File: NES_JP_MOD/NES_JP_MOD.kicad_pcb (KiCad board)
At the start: 2 copper layers, 9 parts, among them J1 Conn_01x06, U1 XC2C64A, U2 AMS1117-1.8, U3 AMS1117-3.3, X1 ASV-xxxMHz

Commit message: Created PCB
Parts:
- added C5: 0.1u, Capacitor_SMD:C_0805_2012Metric, F.Cu at (129.3, 89.2)
- added C6: 0.1u, Capacitor_SMD:C_0805_2012Metric, F.Cu at (129.3, 93.7)
- added C7: 0.1u, Capacitor_SMD:C_0805_2012Metric, F.Cu at (138.4, 98.0)
- added C8: 0.1u, Capacitor_SMD:C_0805_2012Metric, F.Cu at (147.3, 92.2)
- added C9: 0.1u, Capacitor_SMD:C_0805_2012Metric, F.Cu at (133.3, 87.6)
- added Q1: MMBT3904, Package_TO_SOT_SMD:SOT-23, F.Cu at (152.4, 78.7)
- added R1: 5K6, Resistor_SMD:R_0805_2012Metric, F.Cu at (151.9, 83.8)
- added R10: 10K, Resistor_SMD:R_0805_2012Metric, F.Cu at (143.0, 102.1)
- added R11: 10K, Resistor_SMD:R_0805_2012Metric, F.Cu at (139.0, 102.1)
- added R12: 5K6, Resistor_SMD:R_0805_2012Metric, F.Cu at (152.7, 91.2)
- added R13: 10K, Resistor_SMD:R_0805_2012Metric, F.Cu at (150.4, 91.2)
- added R14: 10K, Resistor_SMD:R_0805_2012Metric, F.Cu at (134.9, 102.1)
- added R15: 10K, Resistor_SMD:R_0805_2012Metric, F.Cu at (130.8, 102.1)
- added R16: 10K, Resistor_SMD:R_0805_2012Metric, F.Cu at (126.7, 102.1)
- added R17: 10K, Resistor_SMD:R_0805_2012Metric, F.Cu at (122.7, 102.1)
- added R18: 10K, Resistor_SMD:R_0805_2012Metric, F.Cu at (118.6, 102.1)
- added R2: 10K, Resistor_SMD:R_0805_2012Metric, F.Cu at (149.2, 78.5)
- added R3: 10K, Resistor_SMD:R_0805_2012Metric, F.Cu at (154.9, 97.8)
- added R4: 10K, Resistor_SMD:R_0805_2012Metric, F.Cu at (157.5, 97.8)
- added R5: 10K, Resistor_SMD:R_0805_2012Metric, F.Cu at (156.7, 102.1)
- added R6: 10K, Resistor_SMD:R_0805_2012Metric, F.Cu at (152.7, 102.1)
- added R7: 10K, Resistor_SMD:R_0805_2012Metric, F.Cu at (148.6, 102.1)
- added R8: 5K6, Resistor_SMD:R_0805_2012Metric, F.Cu at (151.9, 88.1)
- added R9: 10K, Resistor_SMD:R_0805_2012Metric, F.Cu at (148.1, 88.1)
- added TP1: TestPoint, TestPoint:TestPoint_Pad_2.0x2.0mm, F.Cu at (157.5, 78.7)
- added TP10: TestPoint, TestPoint:TestPoint_Pad_2.0x2.0mm, F.Cu at (152.1, 105.7)
- added TP11: TestPoint, TestPoint:TestPoint_Pad_2.0x2.0mm, F.Cu at (156.0, 105.7)
- added TP12: TestPoint, TestPoint:TestPoint_Pad_2.0x2.0mm, F.Cu at (157.5, 94.0)
- added TP13: TestPoint, TestPoint:TestPoint_Pad_2.0x2.0mm, F.Cu at (157.5, 90.2)
- added TP14: TestPoint, TestPoint:TestPoint_Pad_2.0x2.0mm, F.Cu at (157.5, 82.5)
- added TP15: TestPoint, TestPoint:TestPoint_Pad_2.0x2.0mm, F.Cu at (157.5, 86.4)
- added TP16: TestPoint, TestPoint:TestPoint_Pad_2.0x2.0mm, F.Cu at (125.0, 78.7)
- added TP17: TestPoint, TestPoint:TestPoint_Pad_2.0x2.0mm, F.Cu at (120.7, 78.7)
- added TP2: TestPoint, TestPoint:TestPoint_Pad_2.0x2.0mm, F.Cu at (119.6, 105.7)
- added TP3: TestPoint, TestPoint:TestPoint_Pad_2.0x2.0mm, F.Cu at (123.4, 105.7)
- added TP4: TestPoint, TestPoint:TestPoint_Pad_2.0x2.0mm, F.Cu at (127.3, 105.7)
- added TP5: TestPoint, TestPoint:TestPoint_Pad_2.0x2.0mm, F.Cu at (131.1, 105.7)
- added TP6: TestPoint, TestPoint:TestPoint_Pad_2.0x2.0mm, F.Cu at (134.9, 105.7)
- added TP7: TestPoint, TestPoint:TestPoint_Pad_2.0x2.0mm, F.Cu at (139.2, 105.7)
- added TP8: TestPoint, TestPoint:TestPoint_Pad_2.0x2.0mm, F.Cu at (143.0, 105.7)
- added TP9: TestPoint, TestPoint:TestPoint_Pad_2.0x2.0mm, F.Cu at (148.3, 105.7)
- moved C1 34.0 mm to (149.2, 83.8), turned to -90 degrees
- moved J1 28.2 mm to (118.1, 83.8)
- moved C3 23.1 mm to (138.7, 83.8), turned to -90 degrees
- moved X1 22.5 mm to (124.5, 91.2), turned to -90 degrees
- moved C2 21.1 mm to (136.4, 83.8), turned to -90 degrees
- moved C4 20.6 mm to (125.3, 83.6), turned to -90 degrees
- moved U2 19.6 mm to (143.8, 81.3), turned to 90 degrees
- moved U3 18.5 mm to (131.3, 81.3), turned to 90 degrees
- moved U1 16.4 mm to (139.2, 92.5)
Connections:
- C4 pad 1: +3.3V -> +3V3
- J1 pad 1: +3.3V -> +3V3
- U1 pad 1: unconnected-(U1-Pad1) -> /CLK
- U1 pad 10: unconnected-(U1-Pad10) -> /BTN6
- U1 pad 19: unconnected-(U1-Pad19) -> +3V3
- U1 pad 24: unconnected-(U1-Pad24) -> /BTN7
- U1 pad 25: unconnected-(U1-Pad25) -> /BTN8
- U1 pad 26: unconnected-(U1-Pad26) -> /BTN9
- U1 pad 27: unconnected-(U1-Pad27) -> /BTN10
- U1 pad 28: unconnected-(U1-Pad28) -> /BTN11
- U1 pad 29: unconnected-(U1-Pad29) -> +1V8
- U1 pad 3: +3.3V -> +3V3
- U1 pad 34: unconnected-(U1-Pad34) -> /LATCH_DIV
- U1 pad 35: unconnected-(U1-Pad35) -> /CLK_DIV
- U1 pad 36: unconnected-(U1-Pad36) -> /DATA_Q
- U1 pad 4: unconnected-(U1-Pad4) -> /BTN0
- U1 pad 42: unconnected-(U1-Pad42) -> +3V3
- U1 pad 5: unconnected-(U1-Pad5) -> /BTN1
- U1 pad 6: unconnected-(U1-Pad6) -> /BTN2
- U1 pad 7: unconnected-(U1-Pad7) -> /BTN3
- U1 pad 8: unconnected-(U1-Pad8) -> /BTN4
- U1 pad 9: unconnected-(U1-Pad9) -> /BTN5
- U3 pad 2: +3.3V -> +3V3
- X1 pad 4: +3.3V -> +3V3
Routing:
- net +3V3: track 0.00 -> 113.0 mm, vias 0 -> 10
- net GND: track 0.00 -> 57.7 mm, vias 0 -> 15
- net /TCK: track 0.00 -> 47.0 mm, vias 0 -> 1
- net +5V: track 0.00 -> 38.7 mm, vias 0 -> 3
- net /TMS: track 0.00 -> 34.7 mm, vias 0 -> 1
- net /TDI: track 0.00 -> 31.9 mm, vias 0 -> 1
- net /TDO: track 0.00 -> 26.7 mm, vias 0 -> 1
- net +1V8: track 0.00 -> 25.7 mm, vias 0 -> 2
- net /BTN0: track 0.00 -> 25.5 mm
- net /BTN1: track 0.00 -> 22.1 mm
- net /BTN11: track 0.00 -> 21.4 mm
- net /BTN9: track 0.00 -> 19.9 mm
- net /BTN10: track 0.00 -> 19.6 mm
- net /BTN2: track 0.00 -> 18.7 mm
- net /BTN6: track 0.00 -> 18.4 mm
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- added copper zone on B.Cu, net +3V3
- added copper zone on B.Cu, net GND
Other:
- board outline added: 43.4 x 31.4 mm

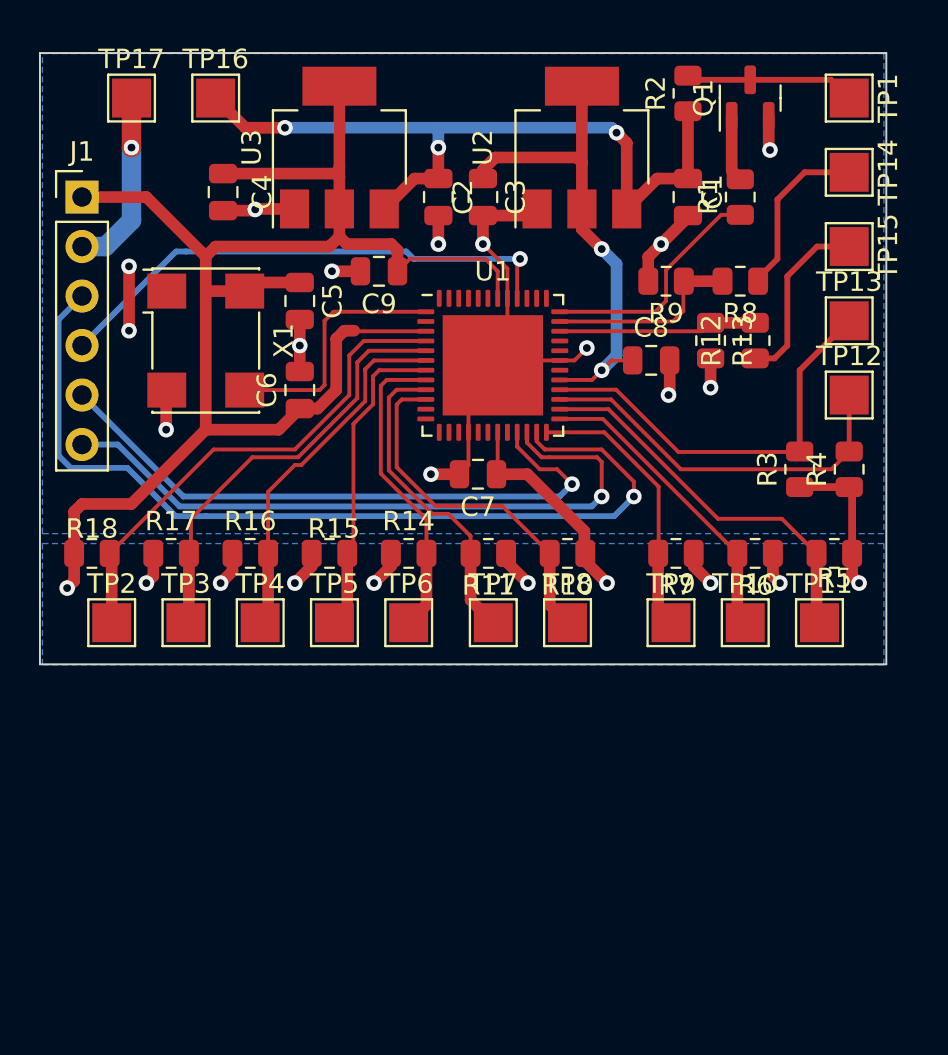
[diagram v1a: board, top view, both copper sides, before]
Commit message: Fixed wrong resistor value
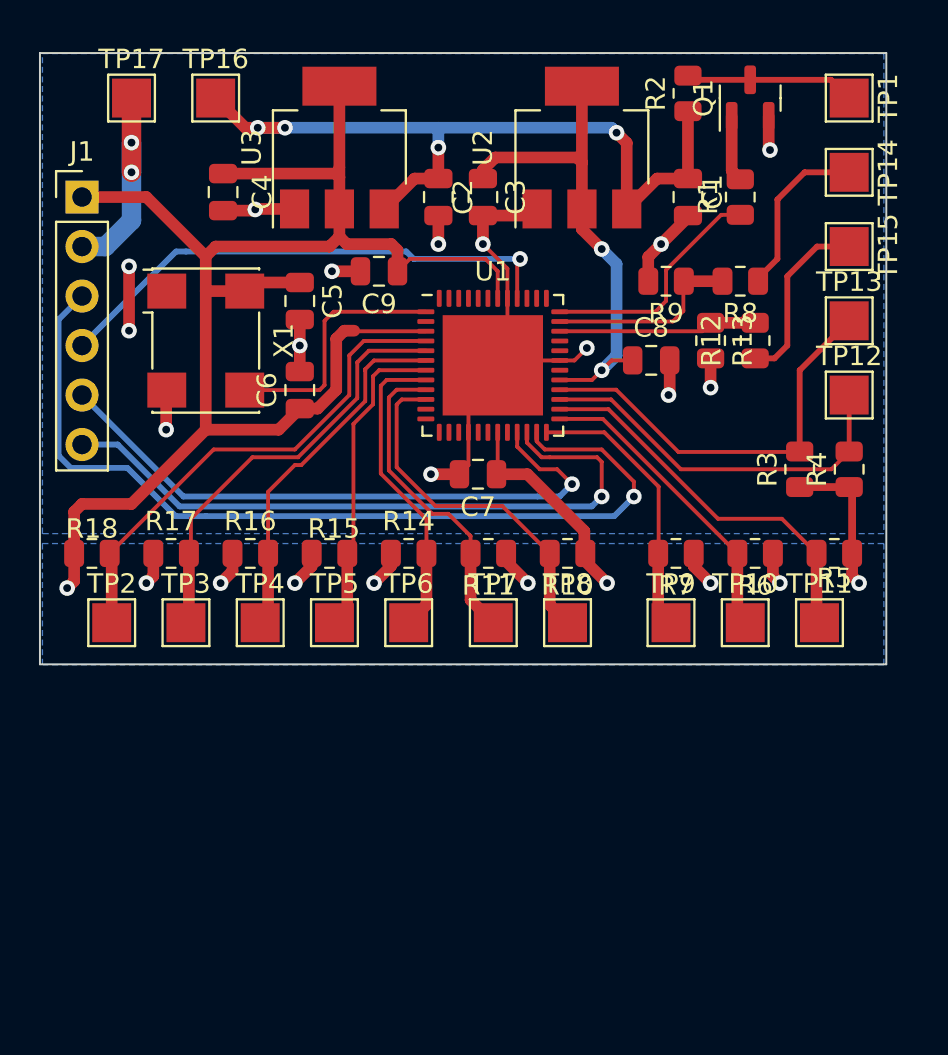
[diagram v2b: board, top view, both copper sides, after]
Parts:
- R2: value 10K -> 1K
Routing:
- net GND: track 57.7 -> 59.2 mm, vias 15 -> 16
- net +5V: track 38.7 -> 40.1 mm, vias 3 -> 4
